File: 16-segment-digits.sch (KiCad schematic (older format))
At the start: 0 parts

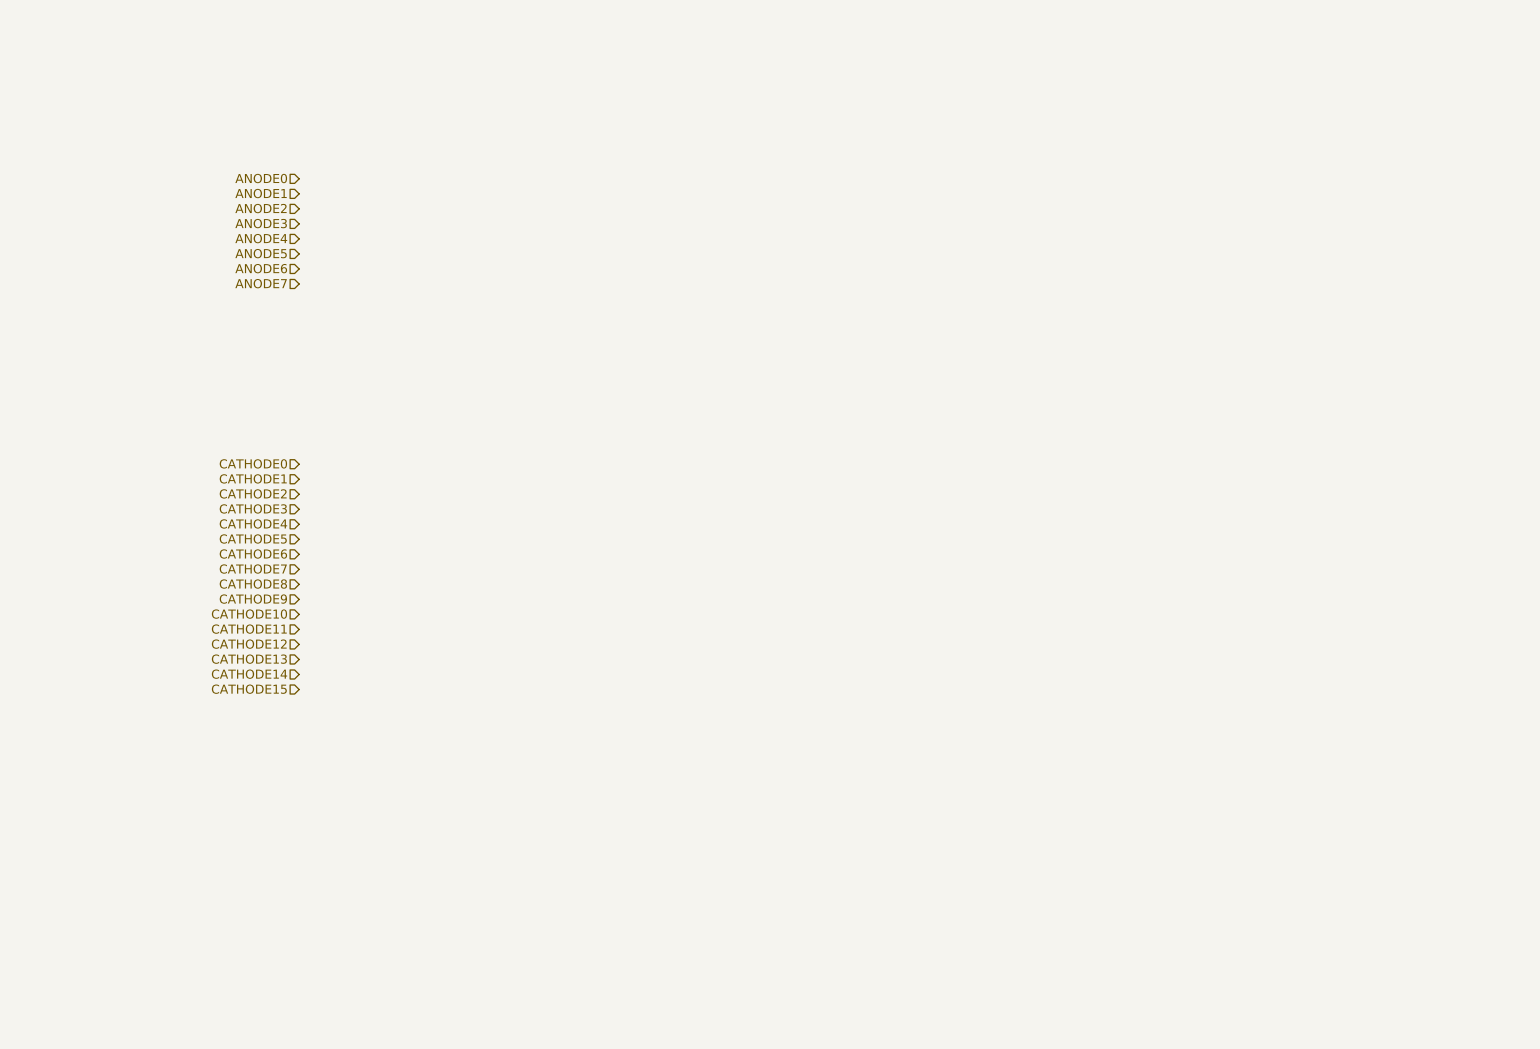
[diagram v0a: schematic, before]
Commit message: I think the layout is finished now. I'll check again after I sleep.
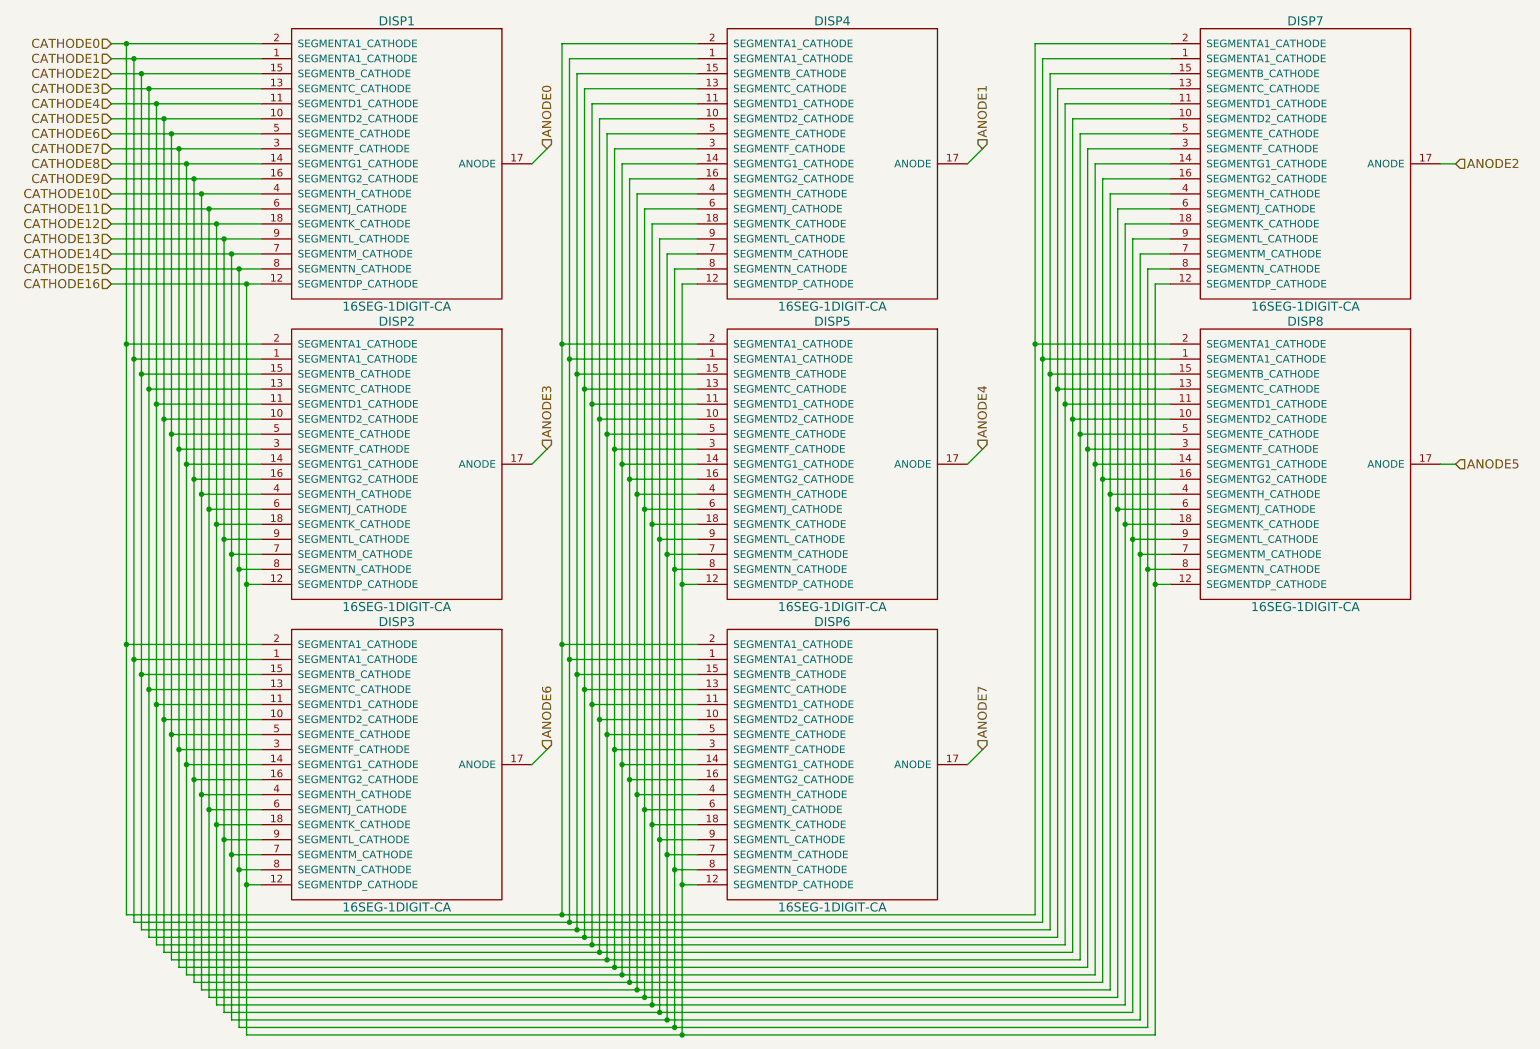
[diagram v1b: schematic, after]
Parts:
- added DISP1, DISP2, DISP3, DISP4, DISP5, DISP6, DISP7, DISP8: 16SEG-1DIGIT-CA, PinballParts:LCSA-8018, symbol 16SEG-1DIGIT-CA
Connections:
- net ANODE0: now also DISP1.17 (ANODE)
- net ANODE1: now also DISP4.17 (ANODE)
- net ANODE2: now also DISP7.17 (ANODE)
- net ANODE3: now also DISP2.17 (ANODE)
- net ANODE4: now also DISP5.17 (ANODE)
- net ANODE5: now also DISP8.17 (ANODE)
- net ANODE6: now also DISP3.17 (ANODE)
- net ANODE7: now also DISP6.17 (ANODE)
- net CATHODE0: now also DISP1.2 (SEGMENTA1_CATHODE), DISP2.2 (SEGMENTA1_CATHODE), DISP3.2 (SEGMENTA1_CATHODE), DISP4.2 (SEGMENTA1_CATHODE), DISP5.2 (SEGMENTA1_CATHODE), DISP6.2 (SEGMENTA1_CATHODE), DISP7.2 (SEGMENTA1_CATHODE), DISP8.2 (SEGMENTA1_CATHODE)
- net CATHODE1: now also DISP1.1 (SEGMENTA1_CATHODE), DISP2.1 (SEGMENTA1_CATHODE), DISP3.1 (SEGMENTA1_CATHODE), DISP4.1 (SEGMENTA1_CATHODE), DISP5.1 (SEGMENTA1_CATHODE), DISP6.1 (SEGMENTA1_CATHODE), DISP7.1 (SEGMENTA1_CATHODE), DISP8.1 (SEGMENTA1_CATHODE)
- net CATHODE10: now also DISP1.4 (SEGMENTH_CATHODE), DISP2.4 (SEGMENTH_CATHODE), DISP3.4 (SEGMENTH_CATHODE), DISP4.4 (SEGMENTH_CATHODE), DISP5.4 (SEGMENTH_CATHODE), DISP6.4 (SEGMENTH_CATHODE), DISP7.4 (SEGMENTH_CATHODE), DISP8.4 (SEGMENTH_CATHODE)
- net CATHODE11: now also DISP1.6 (SEGMENTJ_CATHODE), DISP2.6 (SEGMENTJ_CATHODE), DISP3.6 (SEGMENTJ_CATHODE), DISP4.6 (SEGMENTJ_CATHODE), DISP5.6 (SEGMENTJ_CATHODE), DISP6.6 (SEGMENTJ_CATHODE), DISP7.6 (SEGMENTJ_CATHODE), DISP8.6 (SEGMENTJ_CATHODE)
- net CATHODE12: now also DISP1.18 (SEGMENTK_CATHODE), DISP2.18 (SEGMENTK_CATHODE), DISP3.18 (SEGMENTK_CATHODE), DISP4.18 (SEGMENTK_CATHODE), DISP5.18 (SEGMENTK_CATHODE), DISP6.18 (SEGMENTK_CATHODE), DISP7.18 (SEGMENTK_CATHODE), DISP8.18 (SEGMENTK_CATHODE)
- net CATHODE13: now also DISP1.9 (SEGMENTL_CATHODE), DISP2.9 (SEGMENTL_CATHODE), DISP3.9 (SEGMENTL_CATHODE), DISP4.9 (SEGMENTL_CATHODE), DISP5.9 (SEGMENTL_CATHODE), DISP6.9 (SEGMENTL_CATHODE), DISP7.9 (SEGMENTL_CATHODE), DISP8.9 (SEGMENTL_CATHODE)
- net CATHODE14: now also DISP1.7 (SEGMENTM_CATHODE), DISP2.7 (SEGMENTM_CATHODE), DISP3.7 (SEGMENTM_CATHODE), DISP4.7 (SEGMENTM_CATHODE), DISP5.7 (SEGMENTM_CATHODE), DISP6.7 (SEGMENTM_CATHODE), DISP7.7 (SEGMENTM_CATHODE), DISP8.7 (SEGMENTM_CATHODE)
- net CATHODE15: now also DISP1.8 (SEGMENTN_CATHODE), DISP2.8 (SEGMENTN_CATHODE), DISP3.8 (SEGMENTN_CATHODE), DISP4.8 (SEGMENTN_CATHODE), DISP5.8 (SEGMENTN_CATHODE), DISP6.8 (SEGMENTN_CATHODE), DISP7.8 (SEGMENTN_CATHODE), DISP8.8 (SEGMENTN_CATHODE)
- net CATHODE2: now also DISP1.15 (SEGMENTB_CATHODE), DISP2.15 (SEGMENTB_CATHODE), DISP3.15 (SEGMENTB_CATHODE), DISP4.15 (SEGMENTB_CATHODE), DISP5.15 (SEGMENTB_CATHODE), DISP6.15 (SEGMENTB_CATHODE), DISP7.15 (SEGMENTB_CATHODE), DISP8.15 (SEGMENTB_CATHODE)
- net CATHODE3: now also DISP1.13 (SEGMENTC_CATHODE), DISP2.13 (SEGMENTC_CATHODE), DISP3.13 (SEGMENTC_CATHODE), DISP4.13 (SEGMENTC_CATHODE), DISP5.13 (SEGMENTC_CATHODE), DISP6.13 (SEGMENTC_CATHODE), DISP7.13 (SEGMENTC_CATHODE), DISP8.13 (SEGMENTC_CATHODE)
- net CATHODE4: now also DISP1.11 (SEGMENTD1_CATHODE), DISP2.11 (SEGMENTD1_CATHODE), DISP3.11 (SEGMENTD1_CATHODE), DISP4.11 (SEGMENTD1_CATHODE), DISP5.11 (SEGMENTD1_CATHODE), DISP6.11 (SEGMENTD1_CATHODE), DISP7.11 (SEGMENTD1_CATHODE), DISP8.11 (SEGMENTD1_CATHODE)
- net CATHODE5: now also DISP1.10 (SEGMENTD2_CATHODE), DISP2.10 (SEGMENTD2_CATHODE), DISP3.10 (SEGMENTD2_CATHODE), DISP4.10 (SEGMENTD2_CATHODE), DISP5.10 (SEGMENTD2_CATHODE), DISP6.10 (SEGMENTD2_CATHODE), DISP7.10 (SEGMENTD2_CATHODE), DISP8.10 (SEGMENTD2_CATHODE)
- net CATHODE6: now also DISP1.5 (SEGMENTE_CATHODE), DISP2.5 (SEGMENTE_CATHODE), DISP3.5 (SEGMENTE_CATHODE), DISP4.5 (SEGMENTE_CATHODE), DISP5.5 (SEGMENTE_CATHODE), DISP6.5 (SEGMENTE_CATHODE), DISP7.5 (SEGMENTE_CATHODE), DISP8.5 (SEGMENTE_CATHODE)
- net CATHODE7: now also DISP1.3 (SEGMENTF_CATHODE), DISP2.3 (SEGMENTF_CATHODE), DISP3.3 (SEGMENTF_CATHODE), DISP4.3 (SEGMENTF_CATHODE), DISP5.3 (SEGMENTF_CATHODE), DISP6.3 (SEGMENTF_CATHODE), DISP7.3 (SEGMENTF_CATHODE), DISP8.3 (SEGMENTF_CATHODE)
- net CATHODE8: now also DISP1.14 (SEGMENTG1_CATHODE), DISP2.14 (SEGMENTG1_CATHODE), DISP3.14 (SEGMENTG1_CATHODE), DISP4.14 (SEGMENTG1_CATHODE), DISP5.14 (SEGMENTG1_CATHODE), DISP6.14 (SEGMENTG1_CATHODE), DISP7.14 (SEGMENTG1_CATHODE), DISP8.14 (SEGMENTG1_CATHODE)
- net CATHODE9: now also DISP1.16 (SEGMENTG2_CATHODE), DISP2.16 (SEGMENTG2_CATHODE), DISP3.16 (SEGMENTG2_CATHODE), DISP4.16 (SEGMENTG2_CATHODE), DISP5.16 (SEGMENTG2_CATHODE), DISP6.16 (SEGMENTG2_CATHODE), DISP7.16 (SEGMENTG2_CATHODE), DISP8.16 (SEGMENTG2_CATHODE)
- new net CATHODE16: DISP1.12 (SEGMENTDP_CATHODE), DISP2.12 (SEGMENTDP_CATHODE), DISP3.12 (SEGMENTDP_CATHODE), DISP4.12 (SEGMENTDP_CATHODE), DISP5.12 (SEGMENTDP_CATHODE), DISP6.12 (SEGMENTDP_CATHODE), DISP7.12 (SEGMENTDP_CATHODE), DISP8.12 (SEGMENTDP_CATHODE)
